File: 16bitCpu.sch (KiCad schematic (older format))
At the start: 0 parts

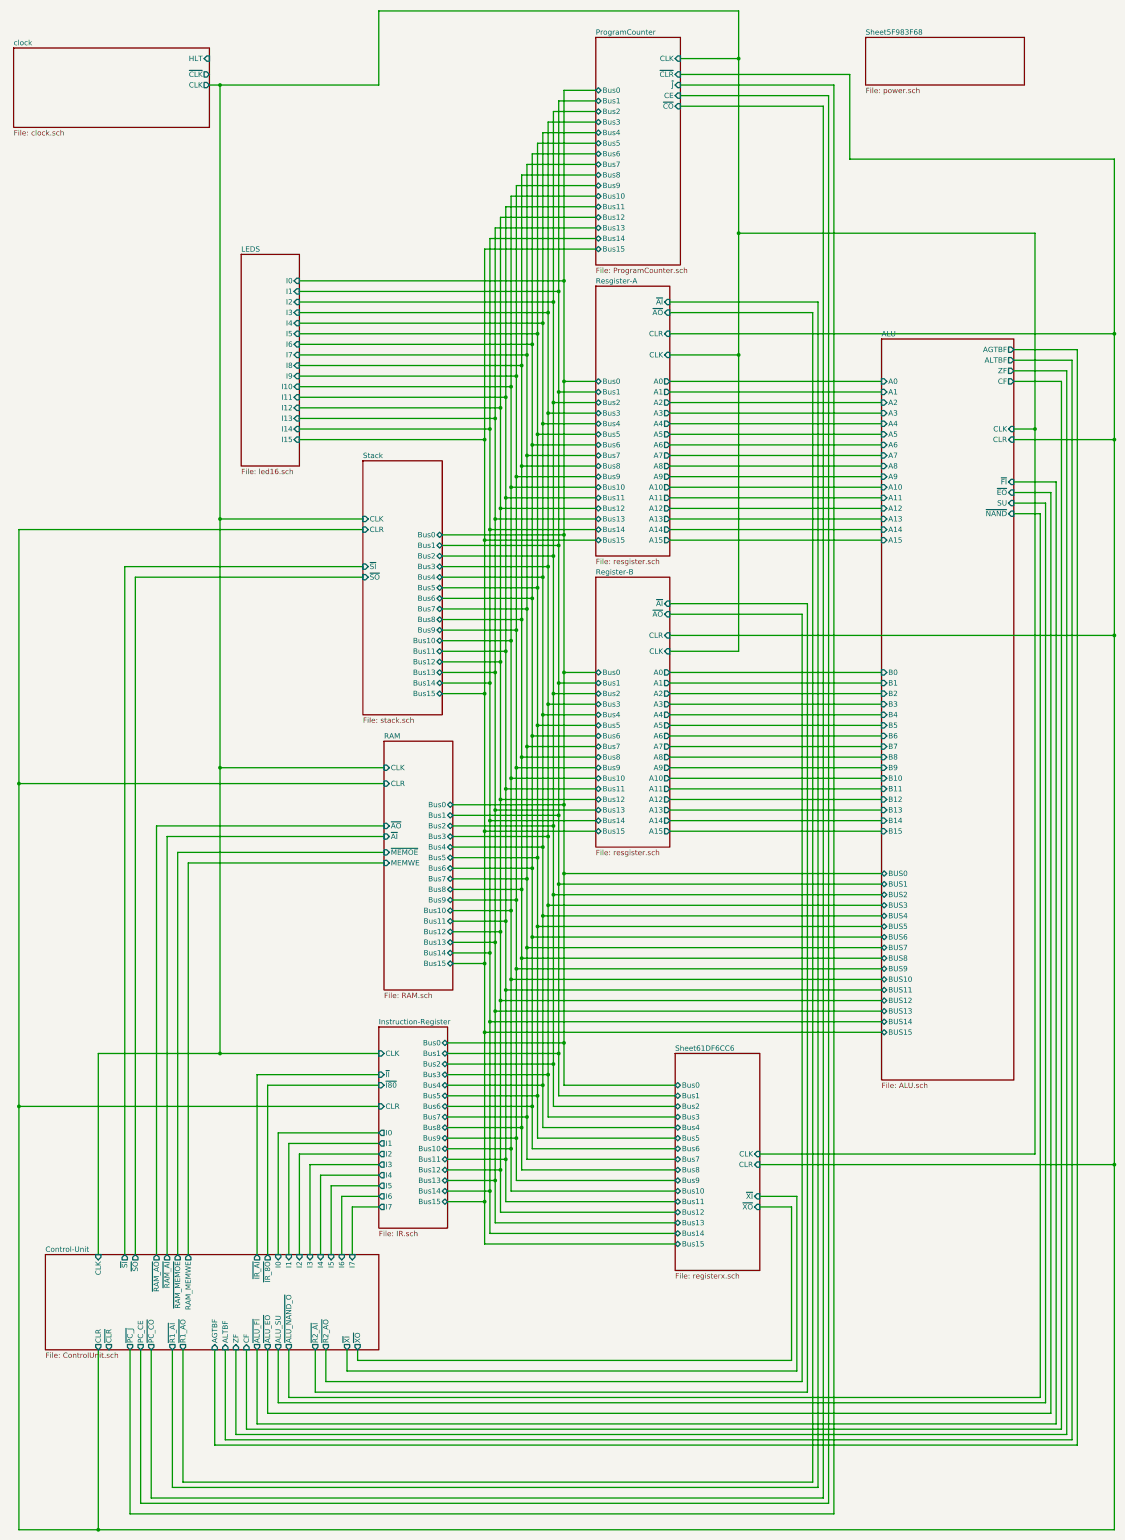
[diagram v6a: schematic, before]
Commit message: added display
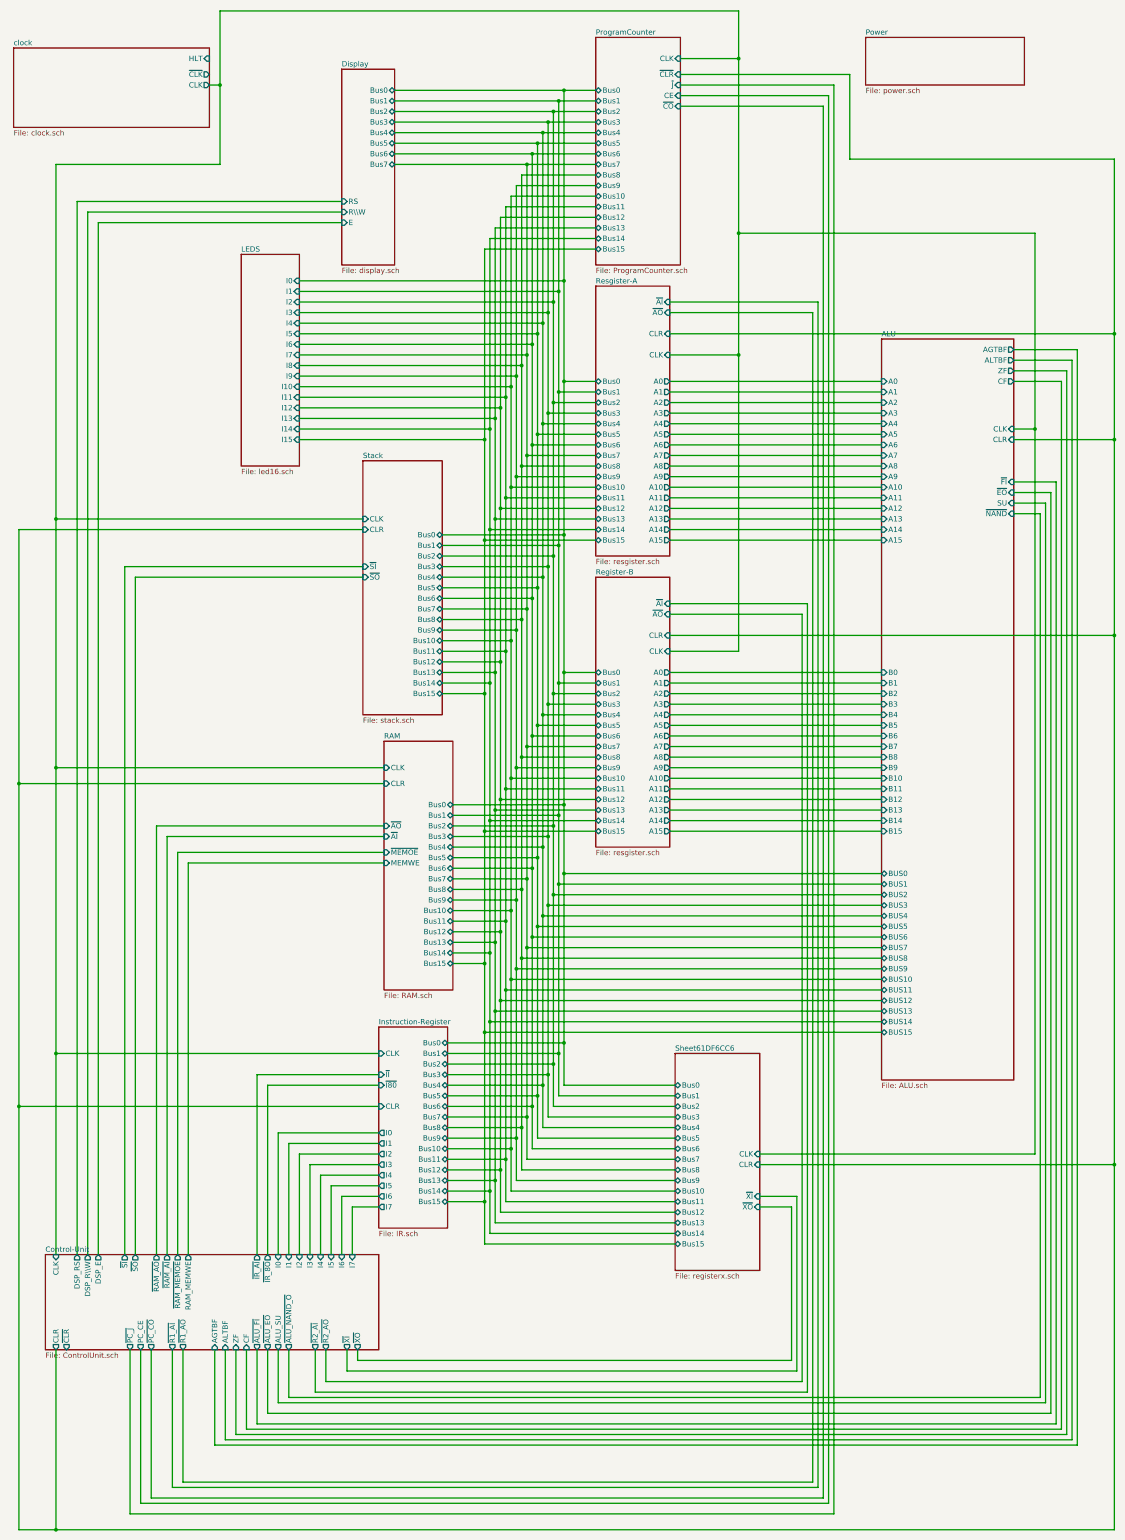
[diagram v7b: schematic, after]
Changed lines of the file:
@@
 $Descr A3 11693 16535 portrait
 encoding utf-8
-Sheet 1 22
+Sheet 1 23
 Title ""
 Date ""
@@
 	6100 1700 5600 1700
 Wire Wire Line
-	6100 1800 5550 1800
-Wire Wire Line
 	6100 2000 5450 2000
 Wire Wire Line
@@
 	5550 1800 5550 3600
 Wire Wire Line
-	5600 1700 5600 3500
-Wire Wire Line
 	5700 1500 5700 3300
 Wire Wire Line
@@
 	6100 1900 5500 1900
 Wire Wire Line
-	4050 550  7450 550
-Wire Wire Line
 	7450 550  7450 1000
 Wire Wire Line
@@
 	10250 4500 10250 11350
 Wire Wire Line
-	4050 550  4050 1250
+	2550 550  2550 1250
 Wire Wire Line
 	2450 1250 2550 1250
 Wire Wire Line
-	2550 1250 2550 5350
-Wire Wire Line
-	2550 5350 3900 5350
-Connection ~ 2550 1250
-Wire Wire Line
-	2550 1250 4050 1250
-Wire Wire Line
-	2550 5350 2550 7700
-Wire Wire Line
-	2550 7700 4100 7700
-Connection ~ 2550 5350
-Wire Wire Line
-	2550 7700 2550 10400
-Wire Wire Line
-	2550 10400 4050 10400
-Connection ~ 2550 7700
-Wire Wire Line
-	2550 10400 1400 10400
-Wire Wire Line
-	1400 10400 1400 12300
-Connection ~ 2550 10400
+	2550 1250 2550 2000
 Connection ~ 10250 4500
 Wire Wire Line
@@
 	2500 14100 2500 13200
 Wire Wire Line
-	1400 13200 1400 14900
-Wire Wire Line
-	1400 14900 11000 14900
+	1000 13200 1000 14900
 Wire Wire Line
 	11000 4600 10050 4600
@@
 	11000 3600 11000 4600
 Wire Wire Line
-	1400 14900 650  14900
-Wire Wire Line
 	650  5450 3900 5450
-Connection ~ 1400 14900
 Wire Wire Line
 	4100 7850 650  7850
@@
 F8 "I6" I T 3700 12300 50
 F9 "I7" I T 3800 12300 50
-F10 "CLK" I T 1400 12300 50
+F10 "CLK" I T 1000 12300 50
 F11 "ZF" I B 2700 13200 50
 F12 "CF" I B 2800 13200 50
@@
 F25 "PC_CE" O B 1800 13200 50
 F26 "~PC_CO" O B 1900 13200 50
-F27 "CLR" O B 1400 13200 50
-F28 "~CLR" O B 1500 13200 50
+F27 "CLR" O B 1000 13200 50
+F28 "~CLR" O B 1100 13200 50
 F29 "~SI" O T 1650 12300 50
 F30 "~SO" O T 1750 12300 50
@@
 F36 "ALTBF" I B 2600 13200 50
 F37 "AGTBF" I B 2500 13200 50
+F38 "DSP_R\\W" O T 1300 12300 50
+F39 "DSP_E" O T 1400 12300 50
+F40 "DSP_RS" O T 1200 12300 50
 $EndSheet
 $Sheet
 S 8650 800  1500 450
 U 5F983F69
-F0 "Sheet5F983F68" 50
+F0 "Power" 50
 F1 "power.sch" 50
 $EndSheet
+$Sheet
+S 3700 1100 500  1850
+U 5FE3FC3C
+F0 "Display" 50
+F1 "display.sch" 50
+F2 "Bus0" T R 4200 1300 50
+F3 "Bus1" T R 4200 1400 50
+F4 "Bus2" T R 4200 1500 50
+F5 "Bus3" T R 4200 1600 50
+F6 "Bus4" T R 4200 1700 50
+F7 "Bus5" T R 4200 1800 50
+F8 "Bus6" T R 4200 1900 50
+F9 "Bus7" T R 4200 2000 50
+F10 "RS" I L 3700 2350 50
+F11 "R\\W" I L 3700 2450 50
+F12 "E" I L 3700 2550 50
+$EndSheet
+Connection ~ 2550 1250
+Wire Wire Line
+	2550 550  7450 550
+Wire Wire Line
+	5800 1300 4200 1300
+Connection ~ 5800 1300
+Wire Wire Line
+	4200 1400 5750 1400
+Connection ~ 5750 1400
+Wire Wire Line
+	5700 1500 4200 1500
+Connection ~ 5700 1500
+Wire Wire Line
+	4200 1600 5650 1600
+Connection ~ 5650 1600
+Wire Wire Line
+	5600 1700 4200 1700
+Connection ~ 5600 1700
+Wire Wire Line
+	5600 1700 5600 3500
+Wire Wire Line
+	6100 1800 5550 1800
+Wire Wire Line
+	5550 1800 4200 1800
+Connection ~ 5550 1800
+Wire Wire Line
+	5500 1900 4200 1900
+Connection ~ 5500 1900
+Wire Wire Line
+	5450 2000 4200 2000
+Connection ~ 5450 2000
+Connection ~ 1000 14900
+Wire Wire Line
+	1000 14900 650  14900
+Wire Wire Line
+	1000 14900 11000 14900
+Wire Wire Line
+	1400 12300 1400 2550
+Wire Wire Line
+	1300 12300 1300 2450
+Wire Wire Line
+	1200 12300 1200 2350
+Wire Wire Line
+	2550 2000 1000 2000
+Wire Wire Line
+	1000 5350 3900 5350
+Wire Wire Line
+	1000 2000 1000 5350
+Connection ~ 1000 5350
+Wire Wire Line
+	4100 7700 1000 7700
+Wire Wire Line
+	1000 5350 1000 7700
+Connection ~ 1000 7700
+Wire Wire Line
+	1000 10400 4050 10400
+Wire Wire Line
+	1000 7700 1000 10400
+Connection ~ 1000 10400
+Wire Wire Line
+	1000 10400 1000 12300
+Wire Wire Line
+	1200 2350 3700 2350
+Wire Wire Line
+	1300 2450 3700 2450
+Wire Wire Line
+	1400 2550 3700 2550
 $EndSCHEMATC

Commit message: added swp_x, and cleanup readme
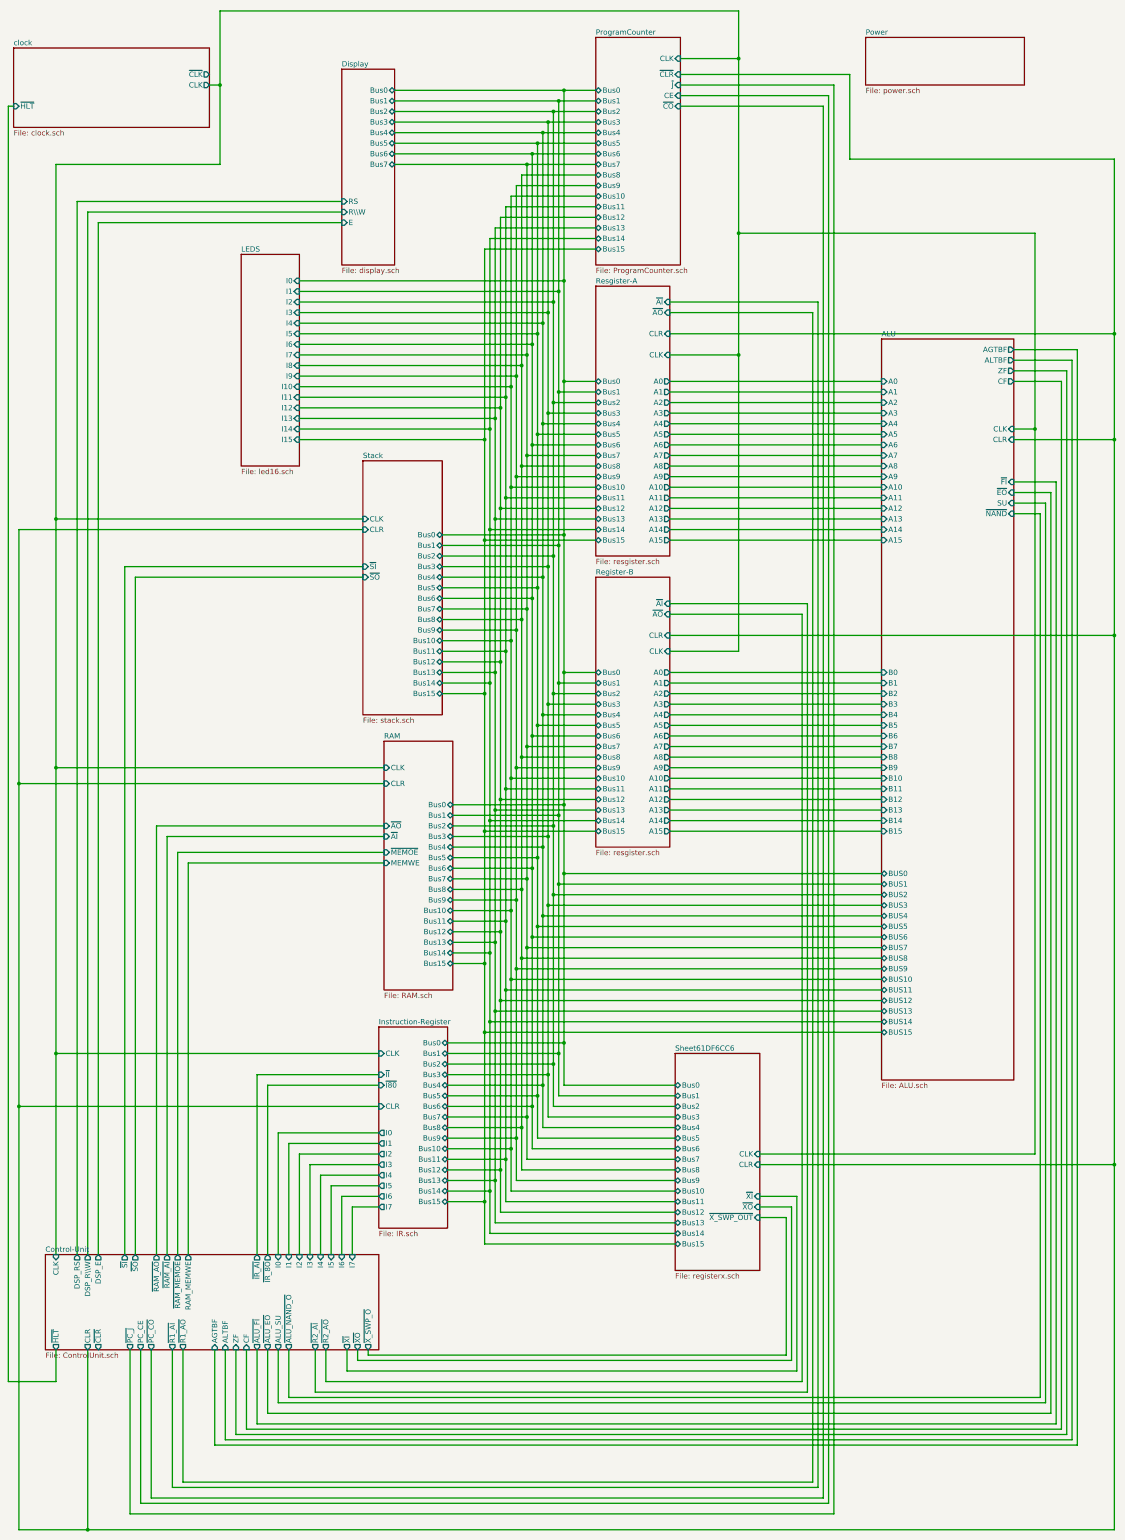
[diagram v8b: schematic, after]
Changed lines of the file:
@@
 F20 "~XO" I R 7650 11850 50
 F21 "Bus15" T L 6850 12200 50
+F22 "~X_SWP_OUT" I R 7650 11950 50
 $EndSheet
 Wire Wire Line
@@
 F0 "clock" 50
 F1 "clock.sch" 50
-F2 "HLT" I R 2450 1000 50
-F3 "~CLK" O R 2450 1150 50
-F4 "CLK" O R 2450 1250 50
+F2 "~CLK" O R 2450 1150 50
+F3 "CLK" O R 2450 1250 50
+F4 "~HLT" I L 600 1450 50
 $EndSheet
 $Sheet
@@
 	2500 14100 2500 13200
 Wire Wire Line
-	1000 13200 1000 14900
+	1300 13200 1300 14900
 Wire Wire Line
 	11000 4600 10050 4600
@@
 F25 "PC_CE" O B 1800 13200 50
 F26 "~PC_CO" O B 1900 13200 50
-F27 "CLR" O B 1000 13200 50
-F28 "~CLR" O B 1100 13200 50
+F27 "CLR" O B 1300 13200 50
+F28 "~CLR" O B 1400 13200 50
 F29 "~SI" O T 1650 12300 50
 F30 "~SO" O T 1750 12300 50
@@
 F39 "DSP_E" O T 1400 12300 50
 F40 "DSP_RS" O T 1200 12300 50
+F41 "~HLT" O B 1000 13200 50
+F42 "~X_SWP_O" O B 3950 13200 50
 $EndSheet
 $Sheet
@@
 	5450 2000 4200 2000
 Connection ~ 5450 2000
-Connection ~ 1000 14900
-Wire Wire Line
-	1000 14900 650  14900
-Wire Wire Line
-	1000 14900 11000 14900
 Wire Wire Line
 	1400 12300 1400 2550
@@
 Wire Wire Line
 	1400 2550 3700 2550
+Connection ~ 1300 14900
+Wire Wire Line
+	1300 14900 11000 14900
+Wire Wire Line
+	650  14900 1300 14900
+Wire Wire Line
+	1000 13200 1000 13500
+Wire Wire Line
+	1000 13500 550  13500
+Wire Wire Line
+	550  13500 550  1450
+Wire Wire Line
+	550  1450 600  1450
+Wire Wire Line
+	7650 11950 7900 11950
+Wire Wire Line
+	7900 11950 7900 13250
+Wire Wire Line
+	7900 13250 3950 13250
+Wire Wire Line
+	3950 13250 3950 13200
 $EndSCHEMATC
